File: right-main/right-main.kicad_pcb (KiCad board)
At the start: 2 copper layers, 150.4 x 123.8 mm, 208 parts, among them J1 USBCONN, P1 CONN_4, P2 CONN_5, P3 CONN_6, SW1 PTS525SM10, SW11 SPST, SW12 SPST, SW13 SPST, SW14 SPST, SW15 SPST, SW16 SPST, SW17 SPST, SW21 SPST, SW22 SPST, SW23 SPST, SW24 SPST, SW25 SPST, SW26 SPST, SW27 SPST, SW31 SPST, SW32 SPST, SW33 SPST, SW34 SPST, SW35 SPST, SW36 SPST, SW37 SPST, SW41 SPST, SW42 SPST, SW43 SPST, SW44 SPST, SW45 SPST, SW46 SPST, SW47 SPST, SW52 SPST, SW53 SPST, SW54 SPST, SW55 SPST, SW56 SPST, SW57 SPST, U1 ATMEGA32U4, U2 CAT24C256, X1 16Mhz

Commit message: switch 32 right
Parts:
- SW32: footprint UGL:Cherry_MX -> ugl:Cherry-MX-Matias-Hybrid
- moved via 38/22mil 2.88 mm to (134.4, 104.4)
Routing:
- net /ROW3: track 185.9 -> 188.4 mm
- net /ROW4: track 217.6 -> 216.7 mm

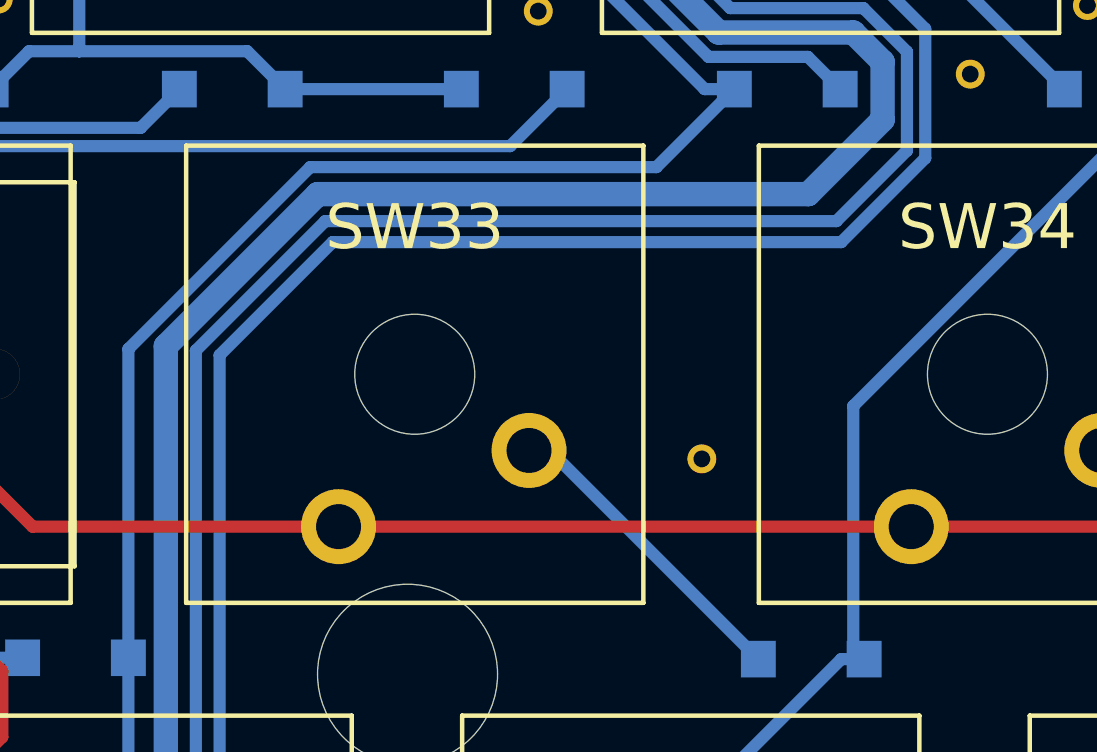
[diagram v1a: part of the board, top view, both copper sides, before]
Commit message: switch 33 right
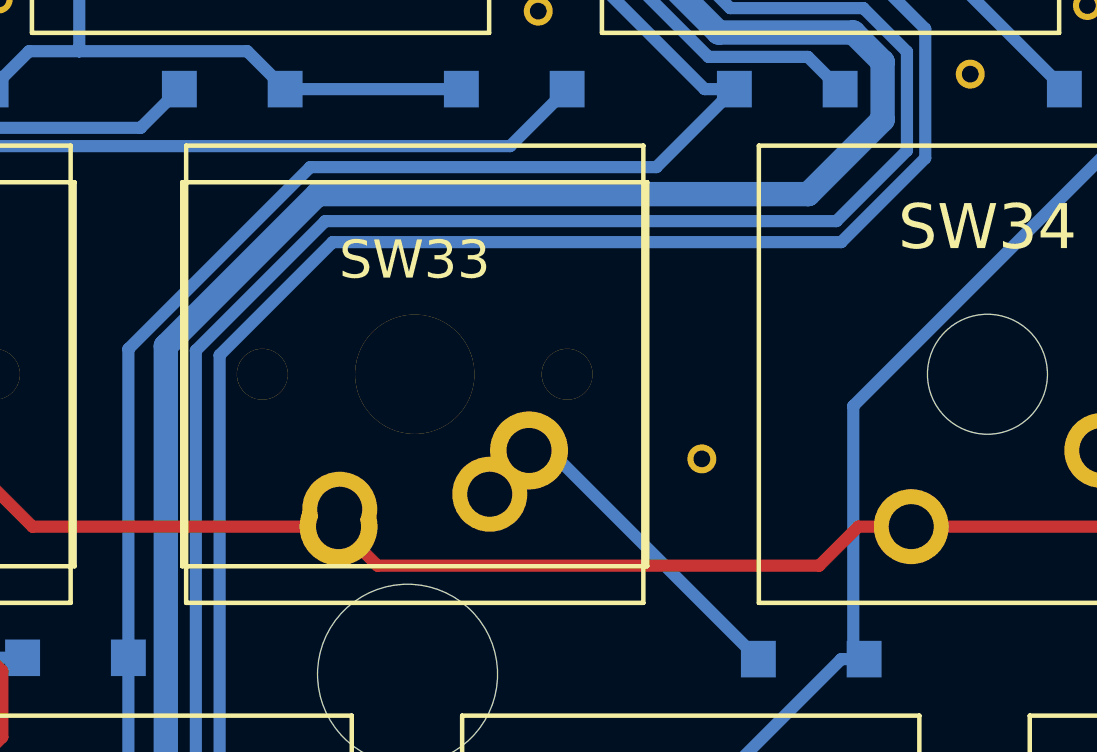
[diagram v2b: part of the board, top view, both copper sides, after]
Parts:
- SW33: footprint UGL:Cherry_MX -> ugl:Cherry-MX-Matias-Hybrid
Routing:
- net Net-(D33-Pad2): track 10.5 -> 12.5 mm
- net /ROW3: track 188.4 -> 189.4 mm
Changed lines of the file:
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@@
 (kicad_pcb (version 4) (host pcbnew 4.0.1-stable)
   (general
-    (links 341)
-    (no_connects 0)
+    (links 343)
+    (no_connects 1)
     (area 19.803 18.9051 270.000001 165.000001)
     (thickness 1.6)
     (drawings 354)
-    (tracks 1035)
+    (tracks 1040)
     (zones 0)
     (modules 208)
@@
     (add_net VCC)
   )
+  (module ugl:Cherry-MX-Matias-Hybrid locked (layer F.Cu)
+    (at 140.250003 101.7 180)
+    (tags switch)
+    (fp_text reference SW32 (at 0 3.81 180) (layer F.SilkS)
+      (effects (font (thickness 0.3048)))
+    )
+    (fp_text value SPST (at 0 0 180) (layer F.SilkS) hide
+      (effects (font (thickness 0.3048)))
+    )
+    (fp_line (start -7.62 7.62) (end -7.62 -7.62) (layer B.SilkS) (width 0.15))
+    (fp_line (start 7.62 7.62) (end -7.62 7.62) (layer B.SilkS) (width 0.15))
+    (fp_line (start 7.62 -7.62) (end 7.62 7.62) (layer B.SilkS) (width 0.15))
+    (fp_line (start -7.62 -7.62) (end 7.62 -7.62) (layer B.SilkS) (width 0.15))
+    (fp_line (start -7.75 -6.4) (end -7.75 6.4) (layer F.SilkS) (width 0.15))
+    (fp_line (start 7.75 -6.4) (end 7.75 6.4) (layer F.SilkS) (width 0.15))
+    (fp_line (start -7.75 6.4) (end 7.75 6.4) (layer F.SilkS) (width 0.15))
+    (fp_line (start -7.75 -6.4) (end 7.75 -6.4) (layer F.SilkS) (width 0.15))
+    (fp_line (start -7.62 -7.62) (end 7.62 -7.62) (layer F.SilkS) (width 0.15))
+    (fp_line (start 7.62 -7.62) (end 7.62 7.62) (layer F.SilkS) (width 0.15))
+    (fp_line (start 7.62 7.62) (end -7.62 7.62) (layer F.SilkS) (width 0.15))
+    (fp_line (start -7.62 7.62) (end -7.62 -7.62) (layer F.SilkS) (width 0.15))
+    (pad 0 thru_hole circle (at 0 0 180) (size 3.98018 3.98018) (drill 3.98018) (layers *.Cu *.Mask F.SilkS))
+    (pad 1 thru_hole circle (at 2.54 -5.08 180) (size 2.6 2.6) (drill 1.5011) (layers *.Cu *.Mask F.SilkS)
+      (net 45 "Net-(D32-Pad2)"))
+    (pad 2 thru_hole circle (at -3.81 -2.54 180) (size 2.6 2.6) (drill 1.5011) (layers *.Cu *.Mask F.SilkS)
+      (net 18 /ROW3))
+    (pad "" thru_hole circle (at -5.08 0 180) (size 1.69926 1.69926) (drill 1.69926) (layers *.Cu *.Mask F.SilkS))
+    (pad "" thru_hole circle (at 5.08 0 180) (size 1.69926 1.69926) (drill 1.69926) (layers *.Cu *.Mask F.SilkS))
+    (pad 1 thru_hole circle (at 2.5 -4.5 180) (size 2.5 2.5) (drill 1.5) (layers *.Cu *.Mask F.SilkS)
+      (net 45 "Net-(D32-Pad2)"))
+    (pad 2 thru_hole circle (at -2.5 -4 180) (size 2.5 2.5) (drill 1.5) (layers *.Cu *.Mask F.SilkS)
+      (net 18 /ROW3))
+    (model cherry_mx1.wrl
+      (at (xyz 0 0 0))
+      (scale (xyz 1 1 1))
+      (rotate (xyz 0 0 0))
+    )
+  )
   (module UGL:SOD-123_Diode (layer B.Cu)
     (at 171.757 92.196)
@@
       (net 18 /ROW3))
   )
-  (module UGL:Cherry_MX locked (layer F.Cu)
-    (at 159.339999 101.7 180)
-    (fp_text reference SW33 (at 0 4.9 180) (layer F.SilkS)
-      (effects (font (size 1.5 1.5) (thickness 0.3)))
-    )
-    (fp_text value SPST (at 0 0 180) (layer F.SilkS) hide
-      (effects (font (size 1.5 1.5) (thickness 0.3)))
-    )
-    (fp_line (start -7.6 -7.6) (end -7.6 7.6) (layer B.SilkS) (width 0.15))
-    (fp_line (start -7.6 7.6) (end 7.6 7.6) (layer B.SilkS) (width 0.15))
-    (fp_line (start 7.6 -7.6) (end 7.6 7.6) (layer B.SilkS) (width 0.15))
-    (fp_line (start -7.6 -7.6) (end 7.6 -7.6) (layer B.SilkS) (width 0.15))
-    (fp_line (start -7.62 -7.62) (end 7.62 -7.62) (layer F.SilkS) (width 0.15))
-    (fp_line (start 7.62 -7.62) (end 7.62 7.62) (layer F.SilkS) (width 0.15))
-    (fp_line (start 7.62 7.62) (end -7.62 7.62) (layer F.SilkS) (width 0.15))
-    (fp_line (start -7.62 7.62) (end -7.62 -7.62) (layer F.SilkS) (width 0.15))
-    (pad "" np_thru_hole circle (at 0 0 180) (size 4 4) (drill 4) (layers *.Cu *.Mask F.SilkS))
-    (pad 2 thru_hole circle (at -3.81 -2.54 180) (size 2.5 2.5) (drill 1.5) (layers *.Cu *.Mask F.SilkS)
-      (net 46 "Net-(D33-Pad2)"))
-    (pad 1 thru_hole circle (at 2.54 -5.08 180) (size 2.5 2.5) (drill 1.5) (layers *.Cu *.Mask F.SilkS)
-      (net 18 /ROW3))
-  )
   (module UGL:UX60-MB-5S8 locked (layer F.Cu)
     (at 175.849803 43.601924 85.4)
@@
   )
   (module ugl:Cherry-MX-Matias-Hybrid locked (layer F.Cu)
-    (at 140.250003 101.7 180)
+    (at 159.339999 101.7 180)
     (tags switch)
-    (fp_text reference SW32 (at 0 3.81 180) (layer F.SilkS)
+    (fp_text reference SW33 (at 0 3.81 180) (layer F.SilkS)
       (effects (font (thickness 0.3048)))
     )
@@
     (pad 0 thru_hole circle (at 0 0 180) (size 3.98018 3.98018) (drill 3.98018) (layers *.Cu *.Mask F.SilkS))
     (pad 1 thru_hole circle (at 2.54 -5.08 180) (size 2.6 2.6) (drill 1.5011) (layers *.Cu *.Mask F.SilkS)
-      (net 45 "Net-(D32-Pad2)"))
-    (pad 2 thru_hole circle (at -3.81 -2.54 180) (size 2.6 2.6) (drill 1.5011) (layers *.Cu *.Mask F.SilkS)
       (net 18 /ROW3))
+    (pad 2 thru_hole circle (at -3.81 -2.54 180) (size 2.6 2.6) (drill 1.5011) (layers *.Cu *.Mask F.SilkS)
+      (net 46 "Net-(D33-Pad2)"))
     (pad "" thru_hole circle (at -5.08 0 180) (size 1.69926 1.69926) (drill 1.69926) (layers *.Cu *.Mask F.SilkS))
     (pad "" thru_hole circle (at 5.08 0 180) (size 1.69926 1.69926) (drill 1.69926) (layers *.Cu *.Mask F.SilkS))
     (pad 1 thru_hole circle (at 2.5 -4.5 180) (size 2.5 2.5) (drill 1.5) (layers *.Cu *.Mask F.SilkS)
-      (net 45 "Net-(D32-Pad2)"))
-    (pad 2 thru_hole circle (at -2.5 -4 180) (size 2.5 2.5) (drill 1.5) (layers *.Cu *.Mask F.SilkS)
       (net 18 /ROW3))
+    (pad 2 thru_hole circle (at -2.5 -4 180) (size 2.5 2.5) (drill 1.5) (layers *.Cu *.Mask F.SilkS)
+      (net 46 "Net-(D33-Pad2)"))
     (model cherry_mx1.wrl
       (at (xyz 0 0 0))
@@
   (segment (start 223.2279 106.862992) (end 223.2279 112.237) (width 0.4064) (layer B.Cu) (net 17))
   (segment (start 227.66 87.78) (end 230.641 87.78) (width 0.4064) (layer B.Cu) (net 17))
+  (segment (start 175.890003 106.78) (end 174.122237 106.78) (width 0.4064) (layer F.Cu) (net 18))
+  (segment (start 174.122237 106.78) (end 172.822238 108.079999) (width 0.4064) (layer F.Cu) (net 18))
+  (segment (start 158.099998 108.079999) (end 156.799999 106.78) (width 0.4064) (layer F.Cu) (net 18))
+  (segment (start 172.822238 108.079999) (end 158.099998 108.079999) (width 0.4064) (layer F.Cu) (net 18))
   (segment (start 143.51 100.584) (end 144.060003 100.033997) (width 0.4064) (layer F.Cu) (net 18))
   (segment (start 144.060003 100.033997) (end 144.060003 94.530003) (width 0.4064) (layer F.Cu) (net 18))
@@
   (segment (start 214.07 106.78) (end 194.98 106.78) (width 0.4064) (layer F.Cu) (net 18))
   (segment (start 194.98 106.78) (end 175.890003 106.78) (width 0.4064) (layer F.Cu) (net 18))
-  (segment (start 175.890003 106.78) (end 156.799999 106.78) (width 0.4064) (layer F.Cu) (net 18))
   (segment (start 246.1641 104.3359) (end 246.26 104.24) (width 0.4064) (layer B.Cu) (net 18))
   (segment (start 209.997216 106.78) (end 205.957 110.820216) (width 0.4064) (layer B.Cu) (net 18))
@@
   (segment (start 141.578899 107.449999) (end 145.2793 111.1504) (width 0.4064) (layer B.Cu) (net 45))
   (segment (start 145.2793 111.1504) (end 146.2679 111.1504) (width 0.4064) (layer B.Cu) (net 45))
+  (segment (start 161.839999 105.7) (end 161.839999 105.55) (width 0.4064) (layer B.Cu) (net 46) (status C00000))
+  (segment (start 161.839999 105.55) (end 163.149999 104.24) (width 0.4064) (layer B.Cu) (net 46) (status C00000))
   (segment (start 163.8377 104.24) (end 170.7937 111.196) (width 0.4064) (layer B.Cu) (net 46))
   (segment (start 163.149999 104.24) (end 163.8377 104.24) (width 0.4064) (layer B.Cu) (net 46))

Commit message: switch 34 right
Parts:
- SW34: footprint UGL:Cherry_MX -> ugl:Cherry-MX-Matias-Hybrid
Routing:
- net Net-(D34-Pad2): track 7.57 -> 9.57 mm
- net /COL3: track 213.3 -> 214.9 mm
- net /ROW3: track 189.4 -> 190.5 mm
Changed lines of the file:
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@@
 (kicad_pcb (version 4) (host pcbnew 4.0.1-stable)
   (general
-    (links 343)
-    (no_connects 1)
+    (links 345)
+    (no_connects 3)
     (area 19.803 18.9051 270.000001 165.000001)
     (thickness 1.6)
     (drawings 354)
-    (tracks 1040)
+    (tracks 1050)
     (zones 0)
     (modules 208)
@@
       (net 18 /ROW3))
   )
-  (module UGL:Cherry_MX locked (layer F.Cu)
-    (at 178.430003 101.7 180)
-    (fp_text reference SW34 (at 0 4.9 180) (layer F.SilkS)
-      (effects (font (size 1.5 1.5) (thickness 0.3)))
-    )
-    (fp_text value SPST (at 0 0 180) (layer F.SilkS) hide
-      (effects (font (size 1.5 1.5) (thickness 0.3)))
-    )
-    (fp_line (start -7.6 -7.6) (end -7.6 7.6) (layer B.SilkS) (width 0.15))
-    (fp_line (start -7.6 7.6) (end 7.6 7.6) (layer B.SilkS) (width 0.15))
-    (fp_line (start 7.6 -7.6) (end 7.6 7.6) (layer B.SilkS) (width 0.15))
-    (fp_line (start -7.6 -7.6) (end 7.6 -7.6) (layer B.SilkS) (width 0.15))
-    (fp_line (start -7.62 -7.62) (end 7.62 -7.62) (layer F.SilkS) (width 0.15))
-    (fp_line (start 7.62 -7.62) (end 7.62 7.62) (layer F.SilkS) (width 0.15))
-    (fp_line (start 7.62 7.62) (end -7.62 7.62) (layer F.SilkS) (width 0.15))
-    (fp_line (start -7.62 7.62) (end -7.62 -7.62) (layer F.SilkS) (width 0.15))
-    (pad "" np_thru_hole circle (at 0 0 180) (size 4 4) (drill 4) (layers *.Cu *.Mask F.SilkS))
-    (pad 2 thru_hole circle (at -3.81 -2.54 180) (size 2.5 2.5) (drill 1.5) (layers *.Cu *.Mask F.SilkS)
-      (net 47 "Net-(D34-Pad2)"))
-    (pad 1 thru_hole circle (at 2.54 -5.08 180) (size 2.5 2.5) (drill 1.5) (layers *.Cu *.Mask F.SilkS)
-      (net 18 /ROW3))
-  )
   (module UGL:UX60-MB-5S8 locked (layer F.Cu)
     (at 175.849803 43.601924 85.4)
@@
     )
   )
+  (module ugl:Cherry-MX-Matias-Hybrid locked (layer F.Cu)
+    (at 178.430003 101.7 180)
+    (tags switch)
+    (fp_text reference SW34 (at 0 3.81 180) (layer F.SilkS)
+      (effects (font (thickness 0.3048)))
+    )
+    (fp_text value SPST (at 0 0 180) (layer F.SilkS) hide
+      (effects (font (thickness 0.3048)))
+    )
+    (fp_line (start -7.62 7.62) (end -7.62 -7.62) (layer B.SilkS) (width 0.15))
+    (fp_line (start 7.62 7.62) (end -7.62 7.62) (layer B.SilkS) (width 0.15))
+    (fp_line (start 7.62 -7.62) (end 7.62 7.62) (layer B.SilkS) (width 0.15))
+    (fp_line (start -7.62 -7.62) (end 7.62 -7.62) (layer B.SilkS) (width 0.15))
+    (fp_line (start -7.75 -6.4) (end -7.75 6.4) (layer F.SilkS) (width 0.15))
+    (fp_line (start 7.75 -6.4) (end 7.75 6.4) (layer F.SilkS) (width 0.15))
+    (fp_line (start -7.75 6.4) (end 7.75 6.4) (layer F.SilkS) (width 0.15))
+    (fp_line (start -7.75 -6.4) (end 7.75 -6.4) (layer F.SilkS) (width 0.15))
+    (fp_line (start -7.62 -7.62) (end 7.62 -7.62) (layer F.SilkS) (width 0.15))
+    (fp_line (start 7.62 -7.62) (end 7.62 7.62) (layer F.SilkS) (width 0.15))
+    (fp_line (start 7.62 7.62) (end -7.62 7.62) (layer F.SilkS) (width 0.15))
+    (fp_line (start -7.62 7.62) (end -7.62 -7.62) (layer F.SilkS) (width 0.15))
+    (pad 0 thru_hole circle (at 0 0 180) (size 3.98018 3.98018) (drill 3.98018) (layers *.Cu *.Mask F.SilkS))
+    (pad 1 thru_hole circle (at 2.54 -5.08 180) (size 2.6 2.6) (drill 1.5011) (layers *.Cu *.Mask F.SilkS)
+      (net 18 /ROW3))
+    (pad 2 thru_hole circle (at -3.81 -2.54 180) (size 2.6 2.6) (drill 1.5011) (layers *.Cu *.Mask F.SilkS)
+      (net 47 "Net-(D34-Pad2)"))
+    (pad "" thru_hole circle (at -5.08 0 180) (size 1.69926 1.69926) (drill 1.69926) (layers *.Cu *.Mask F.SilkS))
+    (pad "" thru_hole circle (at 5.08 0 180) (size 1.69926 1.69926) (drill 1.69926) (layers *.Cu *.Mask F.SilkS))
+    (pad 1 thru_hole circle (at 2.5 -4.5 180) (size 2.5 2.5) (drill 1.5) (layers *.Cu *.Mask F.SilkS)
+      (net 18 /ROW3))
+    (pad 2 thru_hole circle (at -2.5 -4 180) (size 2.5 2.5) (drill 1.5) (layers *.Cu *.Mask F.SilkS)
+      (net 47 "Net-(D34-Pad2)"))
+    (model cherry_mx1.wrl
+      (at (xyz 0 0 0))
+      (scale (xyz 1 1 1))
+      (rotate (xyz 0 0 0))
+    )
+  )
   (gr_line (start 120.857 138.196) (end 121.657 137.396) (angle 90) (layer B.SilkS) (width 0.2))
   (gr_line (start 124.457 148.096) (end 124.457 148.296) (angle 90) (layer B.SilkS) (width 0.2))
@@
   (segment (start 151.0203 126.9593) (end 151.0203 130.396) (width 0.4064) (layer B.Cu) (net 2))
   (segment (start 149.7945 111.1504) (end 149.7945 115.4585) (width 0.4064) (layer B.Cu) (net 2))
+  (segment (start 184.5203 92.196) (end 183.5317 92.196) (width 0.4064) (layer B.Cu) (net 3))
+  (segment (start 183.5317 92.196) (end 174.606034 101.121666) (width 0.4064) (layer B.Cu) (net 3))
+  (segment (start 174.606034 101.121666) (end 174.606034 105.072495) (width 0.4064) (layer B.Cu) (net 3))
+  (segment (start 174.606034 105.072495) (end 173.3317 106.346829) (width 0.4064) (layer B.Cu) (net 3))
+  (segment (start 173.3317 106.346829) (end 173.3317 110.18) (width 0.4064) (layer B.Cu) (net 3))
+  (segment (start 173.3317 110.18) (end 174.3203 111.1686) (width 0.4064) (layer B.Cu) (net 3))
+  (segment (start 174.3203 111.1686) (end 174.3203 111.196) (width 0.4064) (layer B.Cu) (net 3))
   (segment (start 235.966 83.872927) (end 236.536031 83.302896) (width 0.4064) (layer B.Cu) (net 3))
   (segment (start 235.882896 81.443969) (end 234.351969 81.443969) (width 0.4064) (layer B.Cu) (net 3))
@@
   (segment (start 164.1203 130.196) (end 164.1203 131.494808) (width 0.4064) (layer B.Cu) (net 3))
   (segment (start 173.957 110.8327) (end 174.3203 111.196) (width 0.4064) (layer B.Cu) (net 3))
-  (segment (start 173.957 102.7593) (end 173.957 110.8327) (width 0.4064) (layer B.Cu) (net 3))
-  (segment (start 184.5203 92.196) (end 173.957 102.7593) (width 0.4064) (layer B.Cu) (net 3))
   (segment (start 173.557 111.196) (end 164.1203 120.6327) (width 0.4064) (layer B.Cu) (net 3))
   (segment (start 164.1203 120.6327) (end 164.1203 130.196) (width 0.4064) (layer B.Cu) (net 3))
@@
   (segment (start 223.2279 106.862992) (end 223.2279 112.237) (width 0.4064) (layer B.Cu) (net 17))
   (segment (start 227.66 87.78) (end 230.641 87.78) (width 0.4064) (layer B.Cu) (net 17))
+  (segment (start 194.98 106.78) (end 193.212234 106.78) (width 0.4064) (layer F.Cu) (net 18))
+  (segment (start 191.912235 108.079999) (end 177.190002 108.079999) (width 0.4064) (layer F.Cu) (net 18))
+  (segment (start 177.190002 108.079999) (end 175.890003 106.78) (width 0.4064) (layer F.Cu) (net 18))
+  (segment (start 193.212234 106.78) (end 191.912235 108.079999) (width 0.4064) (layer F.Cu) (net 18))
   (segment (start 175.890003 106.78) (end 174.122237 106.78) (width 0.4064) (layer F.Cu) (net 18))
   (segment (start 174.122237 106.78) (end 172.822238 108.079999) (width 0.4064) (layer F.Cu) (net 18))
@@
   (segment (start 247.303 105.283) (end 247.303 111.2) (width 0.4064) (layer B.Cu) (net 18))
   (segment (start 214.07 106.78) (end 194.98 106.78) (width 0.4064) (layer F.Cu) (net 18))
-  (segment (start 194.98 106.78) (end 175.890003 106.78) (width 0.4064) (layer F.Cu) (net 18))
   (segment (start 246.1641 104.3359) (end 246.26 104.24) (width 0.4064) (layer B.Cu) (net 18))
   (segment (start 209.997216 106.78) (end 205.957 110.820216) (width 0.4064) (layer B.Cu) (net 18))
@@
   (segment (start 141.578899 107.449999) (end 145.2793 111.1504) (width 0.4064) (layer B.Cu) (net 45))
   (segment (start 145.2793 111.1504) (end 146.2679 111.1504) (width 0.4064) (layer B.Cu) (net 45))
-  (segment (start 161.839999 105.7) (end 161.839999 105.55) (width 0.4064) (layer B.Cu) (net 46) (status C00000))
-  (segment (start 161.839999 105.55) (end 163.149999 104.24) (width 0.4064) (layer B.Cu) (net 46) (status C00000))
+  (segment (start 161.839999 105.7) (end 161.839999 105.55) (width 0.4064) (layer B.Cu) (net 46))
+  (segment (start 161.839999 105.55) (end 163.149999 104.24) (width 0.4064) (layer B.Cu) (net 46))
   (segment (start 163.8377 104.24) (end 170.7937 111.196) (width 0.4064) (layer B.Cu) (net 46))
   (segment (start 163.149999 104.24) (end 163.8377 104.24) (width 0.4064) (layer B.Cu) (net 46))
+  (segment (start 180.930003 105.7) (end 180.930003 105.55) (width 0.4064) (layer B.Cu) (net 47))
+  (segment (start 180.930003 105.55) (end 182.240003 104.24) (width 0.4064) (layer B.Cu) (net 47))
   (segment (start 182.0545 104.425503) (end 182.240003 104.24) (width 0.4064) (layer B.Cu) (net 47))
   (segment (start 183.0937 105.093697) (end 183.0937 111.196) (width 0.4064) (layer B.Cu) (net 47))
